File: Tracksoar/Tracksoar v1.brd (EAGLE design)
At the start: 50.4 x 19.5 mm, 39 parts, among them IC2 74AHC1G125DBV, U1 ATMEGA328P, Y1 16MHZ

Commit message: replace headers
replaced 2.54mm headers on all production boards with 2mm headers to
resolve daughter board issues.
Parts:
- removed FTDI: (no value), SparkFun-Connectors:1X06_NO_SILK
- removed JP2: (no value), SparkFun-Connectors:1X01
- added U$3: 1X7, headers(2mm):1X7
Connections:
- net !RESET: now also U$3.7; no longer JP2.1
- net DTR: now also U$3.6; no longer FTDI.1
- net GND: now also U$3.1, U$3.2; no longer FTDI.5, FTDI.6
- net RXO: now also U$3.4; no longer FTDI.3
- net TXO: now also U$3.5; no longer FTDI.2
- net VCC: now also U$3.3; no longer FTDI.4
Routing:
- net RXO: track 25.1 -> 28.7 mm
- net GND: track 87.6 -> 85.0 mm
- net VCC: track 97.5 -> 99.1 mm
- net TXO: track 13.5 -> 14.7 mm

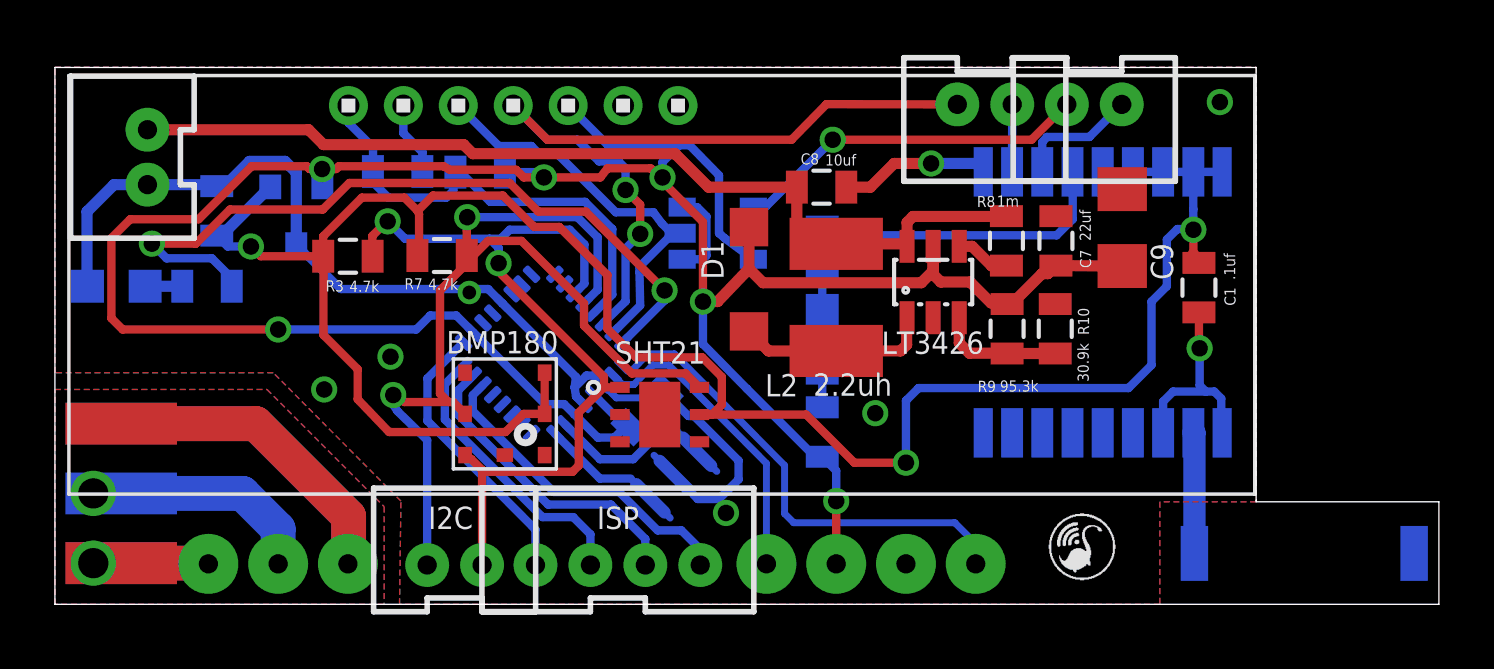
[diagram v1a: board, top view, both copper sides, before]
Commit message: Rounded corners
Added rounded corners to the tracksoar v1
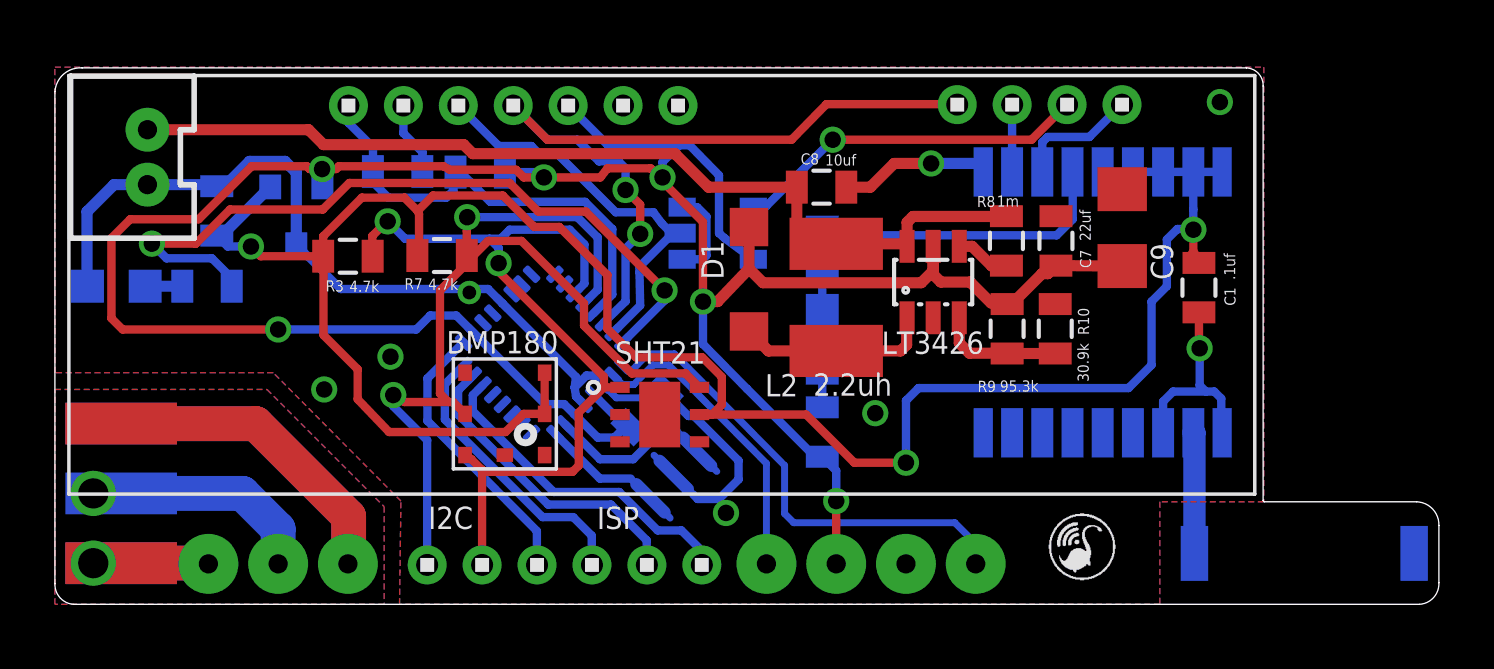
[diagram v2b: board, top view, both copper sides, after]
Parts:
- removed RX: RX, SparkFun-Connectors:JST-2-PTH-VERT
- removed SPI: (no value), SparkFun-Connectors:JST-4-PTH-VERT
- removed TX, TX1: TX, SparkFun-Connectors:JST-2-PTH-VERT
- added SERIAL: 1X4, headers(2mm):1X4
- added SPI/I2C: 1X6, headers(2mm):1X6
- renumbered U$3 to FTDI
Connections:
- net MISO: now also SPI/I2C.4; no longer SPI.2
- net MOSI: now also SPI/I2C.5; no longer SPI.3
- net RX1: now also SERIAL.1; no longer RX.1
- net RXO: now also SERIAL.4; no longer TX.2
- net SCK: now also SPI/I2C.3; no longer SPI.1
- net SCL: now also SPI/I2C.1; no longer TX1.1
- net SDA: now also SPI/I2C.2; no longer TX1.2
- net SS: now also SPI/I2C.6; no longer SPI.4
- net TX: now also SERIAL.3; no longer TX.1
- net TX1: now also SERIAL.2; no longer RX.2
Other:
- outline, holes or cut-outs redrawn

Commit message: fixed silk screen
fixed minor errors and overlaps on the silkscreen
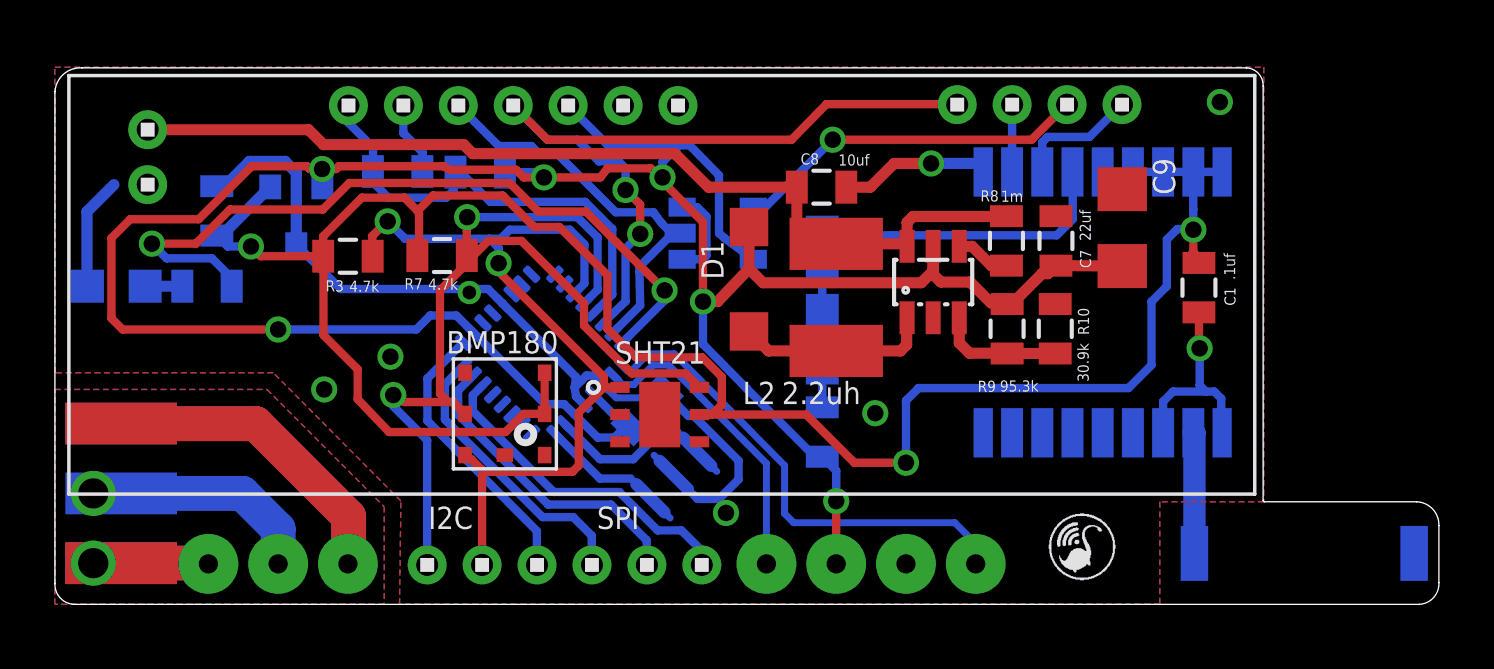
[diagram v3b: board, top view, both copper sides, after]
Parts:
- removed JP1: M02JST-PTH-VERT, SparkFun-Connectors:JST-2-PTH-VERT
- added U$3: 1X2, headers(2mm):1X2
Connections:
- net 15V: now also U$3.2; no longer JP1.2
- net GND: now also U$3.1; no longer JP1.1
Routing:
- net GND: track 85.0 -> 81.3 mm
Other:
- board text added: "SPI"
- board text removed: "ISP"
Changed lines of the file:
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@@
 <text x="0.9144" y="16.8402" size="1.778" layer="26">+</text>
 <text x="2.286" y="14.8082" size="1.778" layer="26" rot="R90">-</text>
-<text x="27.305" y="18.6436" size="0.8128" layer="26" rot="MR180">GND</text>
-<text x="26.0858" y="15.748" size="0.8128" layer="26" rot="MR0">FTDI</text>
+<text x="23.7744" y="18.6944" size="0.8128" layer="26" rot="MR180">GND</text>
+<text x="21.209" y="15.9258" size="0.8128" layer="26" rot="MR0">FTDI</text>
 <text x="13.6144" y="2.7686" size="0.8128" layer="25">I2C</text>
-<text x="19.7612" y="2.7686" size="0.8128" layer="25">ISP</text>
+<text x="19.7612" y="2.7686" size="0.8128" layer="25">SPI</text>
 <rectangle x1="37.3507" y1="0.9017" x2="37.5031" y2="0.9271" layer="25"/>
 <rectangle x1="37.1729" y1="0.9271" x2="37.6809" y2="0.9525" layer="25"/>
@@
 <attribute name="VALUE" x="17.7791625" y="3.97625625" size="0.8128" layer="26" rot="MR45"/>
 </element>
-<element name="JP1" library="SparkFun-Connectors" package="JST-2-PTH-VERT" value="M02JST-PTH-VERT" x="2.8448" y="16.3068" smashed="yes" rot="R90">
-<attribute name="NAME" x="6.175" y="19.0528" size="0.8128" layer="26" rot="MR270"/>
-</element>
 <element name="J$1" library="SparkFun-Connectors" package="SMA-EDGE" value="SMA_EDGE" x="2.4384" y="1.524" smashed="yes" rot="MR90"/>
 <element name="R1" library="SparkFun-Resistors" package="0805" value="100ohm" x="27.9654" y="12.8778" smashed="yes" rot="MR270">
@@
 </element>
 <element name="LT3426" library="adafruit" package="SOT23-6" value="LT3426" x="32.004" y="11.7602" smashed="yes">
-<attribute name="NAME" x="30.1244" y="9.144" size="0.8128" layer="25"/>
-<attribute name="VALUE" x="30.1244" y="9.144" size="0.8128" layer="27"/>
+<attribute name="VALUE" x="30.2006" y="8.8392" size="0.8128" layer="27"/>
 </element>
 <element name="D1" library="diode" package="SOD123" value="MBR120VLSFT1" x="25.2984" y="11.8618" smashed="yes" rot="R270">
@@
 </element>
 <element name="L2" library="resistor" package="L1812" value="2.2uh" x="28.4734" y="11.2014" smashed="yes" rot="R270">
-<attribute name="NAME" x="25.8826" y="7.5946" size="0.8128" layer="25"/>
-<attribute name="VALUE" x="30.5054" y="8.4328" size="0.8128" layer="25" rot="R180"/>
+<attribute name="NAME" x="25.0698" y="7.3152" size="0.8128" layer="25"/>
+<attribute name="VALUE" x="29.3624" y="8.128" size="0.8128" layer="25" rot="R180"/>
 </element>
 <element name="R8" library="SparkFun-Resistors" package="0805" value="1m" x="34.671" y="13.2588" smashed="yes" rot="R90">
-<attribute name="NAME" x="34.2646" y="14.8971" size="0.4064" layer="25" rot="R180"/>
-<attribute name="VALUE" x="35.1282" y="14.9098" size="0.4064" layer="25" rot="R180"/>
+<attribute name="NAME" x="34.3916" y="15.1003" size="0.4064" layer="25" rot="R180"/>
+<attribute name="VALUE" x="35.2806" y="15.0876" size="0.4064" layer="25" rot="R180"/>
 </element>
 <element name="R9" library="SparkFun-Resistors" package="0805" value="95.3k" x="34.6964" y="10.0584" smashed="yes" rot="R90">
@@
 <element name="C8" library="SparkFun-Capacitors" package="0805" value="10uf" x="27.94" y="15.2146" smashed="yes">
 <attribute name="NAME" x="27.178" y="16.0401" size="0.4064" layer="25"/>
-<attribute name="VALUE" x="28.067" y="16.002" size="0.4064" layer="25"/>
+<attribute name="VALUE" x="28.5496" y="16.002" size="0.4064" layer="25"/>
 </element>
 <element name="C9" library="resistor" package="C1206" value="100uf" x="38.8874" y="13.7414" smashed="yes" rot="R90">
-<attribute name="NAME" x="40.7416" y="11.8364" size="0.8128" layer="25" rot="R90"/>
+<attribute name="NAME" x="40.8178" y="14.9352" size="0.8128" layer="25" rot="R90"/>
 <attribute name="VALUE" x="40.7416" y="13.335" size="0.8128" layer="26" rot="R90"/>
 </element>
@@
 <element name="SPI/I2C" library="headers(2mm)" package="1X6" value="1X6" x="18.58" y="1.46"/>
 <element name="SERIAL" library="headers(2mm)" package="1X4" value="1X4" x="35.88" y="18.22" rot="R180"/>
+<element name="U$3" library="headers(2mm)" package="1X2" value="1X2" x="3.4036" y="16.3068" rot="R90"/>
 </elements>
 <signals>
@@
 <contactref element="J$1" pad="GND@1"/>
 <contactref element="J$1" pad="GND@2"/>
-<contactref element="JP1" pad="1"/>
 <contactref element="U$2" pad="0V"/>
 <contactref element="U$2" pad="RFGND2"/>
@@
 <contactref element="LM3480" pad="3"/>
 <contactref element="BMP180" pad="7"/>
-<wire x1="3.3948" y1="15.3068" x2="2.175" y2="15.3068" width="0.4064" layer="16"/>
 <wire x1="2.175" y1="15.3068" x2="1.1938" y2="14.3256" width="0.4064" layer="16"/>
 <wire x1="1.1938" y1="14.3256" x2="1.1938" y2="11.6246" width="0.4064" layer="16"/>
 <wire x1="1.1938" y1="11.6246" x2="1.2106" y2="11.6078" width="0.4064" layer="16"/>
-<wire x1="3.3948" y1="15.3068" x2="5.8624" y2="15.3068" width="0.4064" layer="16"/>
 <wire x1="5.8624" y1="15.3068" x2="5.9182" y2="15.251" width="0.4064" layer="16"/>
 <wire x1="5.9182" y1="15.251" x2="6.2086" y2="15.251" width="0.4064" layer="16"/>
@@
 <contactref element="FTDI" pad="1"/>
 <contactref element="FTDI" pad="2"/>
+<contactref element="U$3" pad="1"/>
 <wire x1="9.8298" y1="7.8486" x2="7.3406" y2="6.604" width="0" layer="19" extent="1-1"/>
 </signal>
@@
 </signal>
 <signal name="15V">
-<contactref element="JP1" pad="2"/>
-<wire x1="3.3948" y1="17.3068" x2="9.2616" y2="17.3068" width="0.4064" layer="1"/>
 <wire x1="9.2616" y1="17.3068" x2="9.8044" y2="16.764" width="0.4064" layer="1"/>
 <wire x1="9.8044" y1="16.764" x2="14.9098" y2="16.764" width="0.4064" layer="1"/>
@@
 <wire x1="31.2674" y1="14.1478" x2="34.66" y2="14.1478" width="0.4064" layer="1"/>
 <wire x1="34.66" y1="14.1478" x2="34.671" y2="14.1588" width="0.4064" layer="1"/>
+<contactref element="U$3" pad="2"/>
+<wire x1="9.2616" y1="17.3068" x2="3.4036" y2="17.3068" width="0.4064" layer="1"/>
 </signal>
 <signal name="N$9">
@@
 </signal>
 </signals>
+<errors>
+</errors>
 </board>
 </drawing>

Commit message: removed components below gps
Removed the step up circuit components below the gps receiver and added
vias to prevent any interference
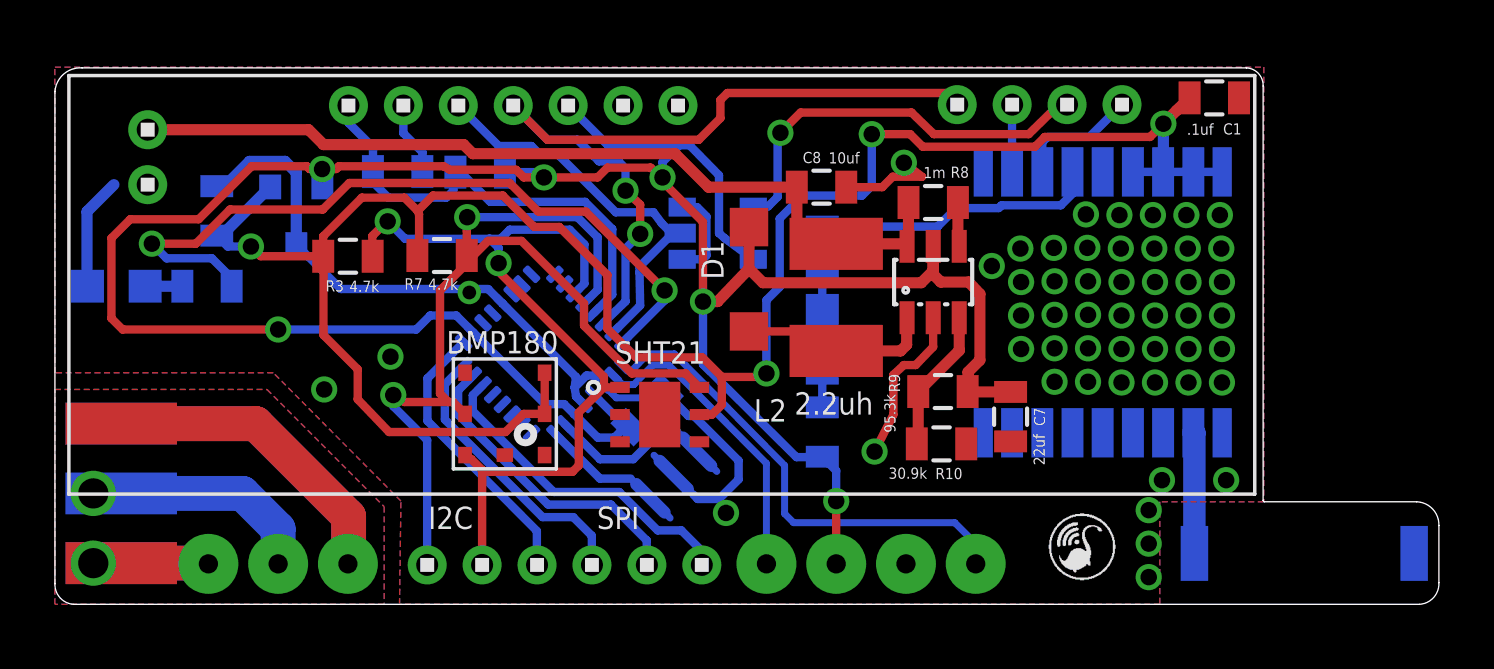
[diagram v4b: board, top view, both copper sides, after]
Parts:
- removed C9: 100uf, resistor:C1206
- moved C1 6.93 mm to (42.2, 18.5), turned to 180 degrees
- moved C7 6.61 mm to (34.8, 6.86), turned to 270 degrees
- moved R10 5.89 mm to (32.3, 5.87), turned to 180 degrees
- moved R9 3.27 mm to (32.4, 7.77), turned to 0 degrees
- moved R8 3.01 mm to (32.0, 14.7), turned to 180 degrees
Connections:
- net GND: no longer C9.2
- net VCC: no longer C9.1
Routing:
- net GND: track 81.3 -> 77.7 mm, vias 9 -> 52
- net 15V: track 34.8 -> 31.8 mm
- net TX1: track 13.0 -> 14.9 mm
- net 3V: track 78.0 -> 76.8 mm, vias 3 -> 4
- net PPS: track 11.2 -> 10.4 mm
- net RXO: track 28.7 -> 29.4 mm
- net N$13: track 4.57 -> 5.23 mm

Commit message: added ground bias
added ground bias to 2 meter antenna connector
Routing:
- net GND: vias 52 -> 58
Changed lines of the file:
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@@
 <via x="38.7858" y="14.1986" extent="1-16" drill="0.6"/>
 <via x="37.5666" y="14.224" extent="1-16" drill="0.6"/>
-<wire x1="9.8298" y1="7.8486" x2="7.3406" y2="6.604" width="0" layer="19" extent="1-1"/>
+<via x="6.2992" y="6.7564" extent="1-16" drill="0.6"/>
+<via x="7.493" y="6.6548" extent="1-16" drill="0.6"/>
+<via x="8.3312" y="5.8166" extent="1-16" drill="0.6"/>
+<via x="9.1694" y="4.9784" extent="1-16" drill="0.6"/>
+<via x="10.0076" y="4.1402" extent="1-16" drill="0.6"/>
+<via x="10.8458" y="3.302" extent="1-16" drill="0.6"/>
+<wire x1="9.8298" y1="7.8486" x2="8.3312" y2="5.8166" width="0" layer="19" extent="1-1"/>
 </signal>
 <signal name="VCC">
